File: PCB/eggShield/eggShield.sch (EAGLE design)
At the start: 34 parts, among them U1 V_REG_LDOSMD, U2 V_REG_LDOSMD

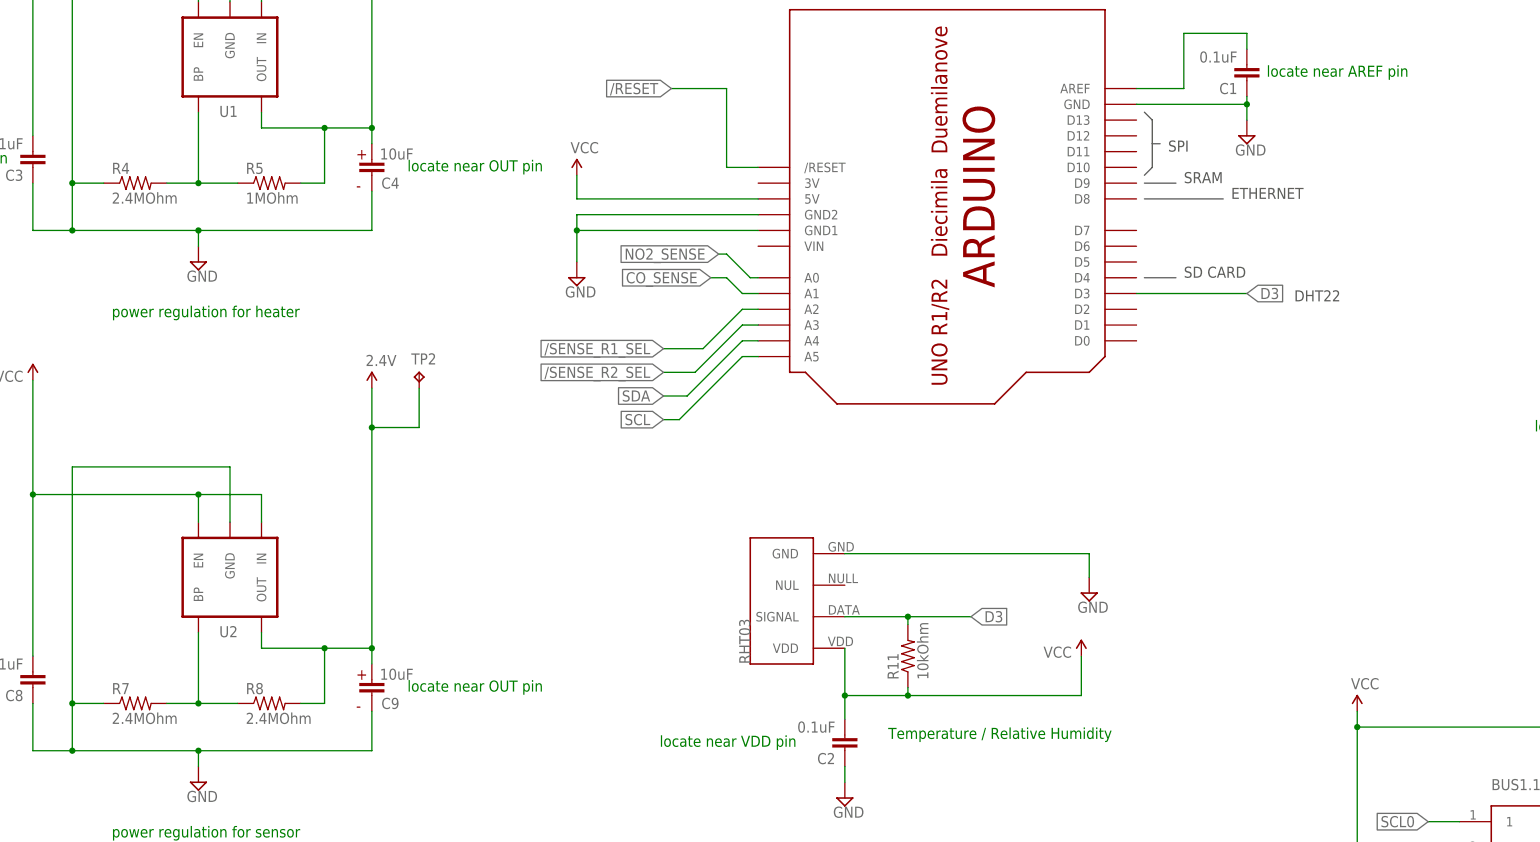
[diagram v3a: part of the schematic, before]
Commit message: changed DHT22 I/O to DIG2, changed LDO feedback resistor values again,  added more documentation to the schematic
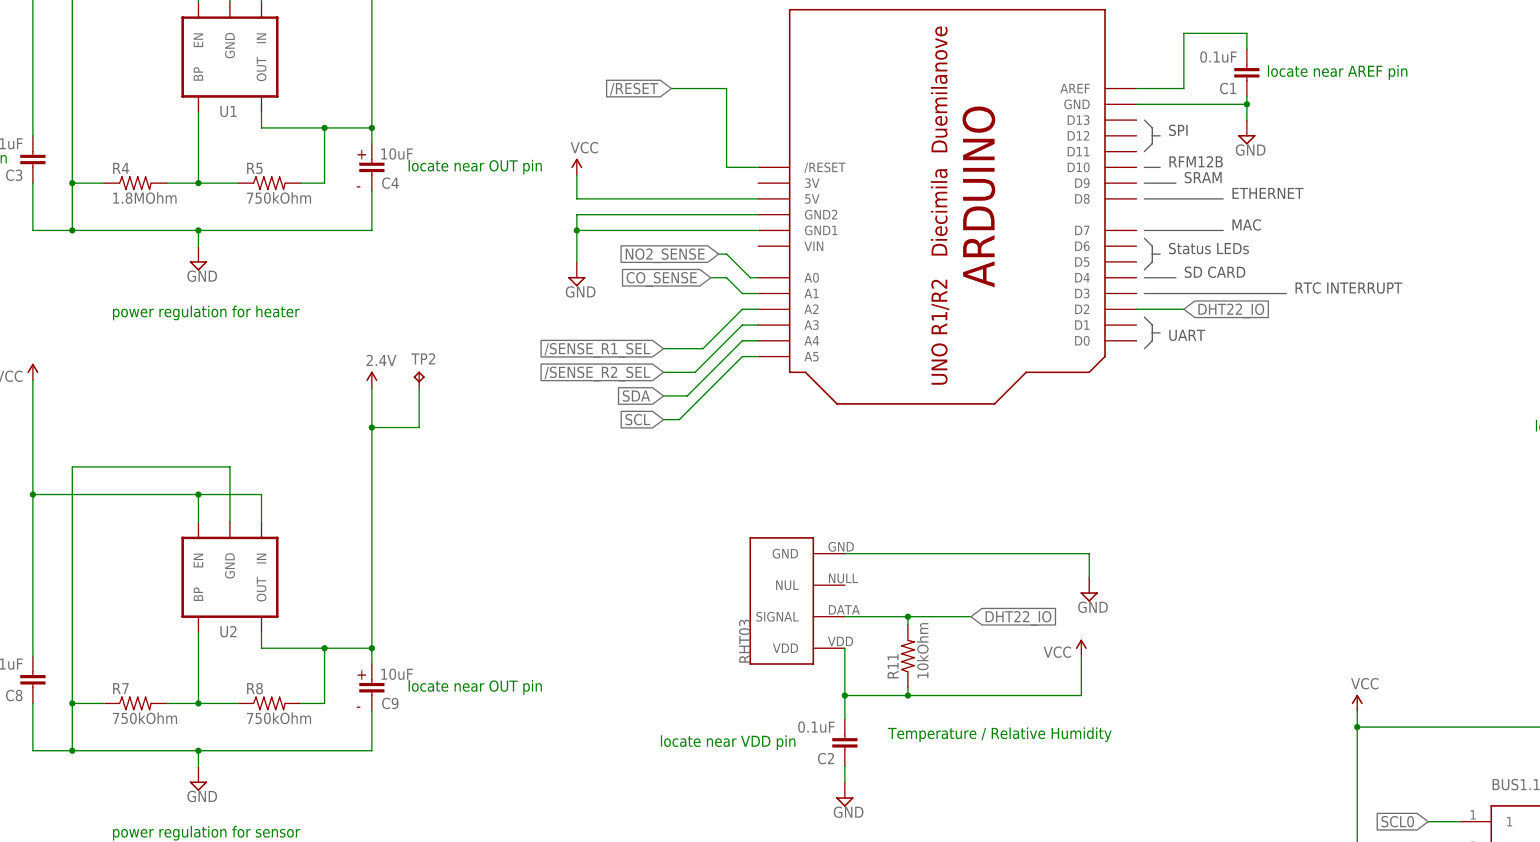
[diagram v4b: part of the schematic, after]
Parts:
- R4: value 2.4MOhm -> 1.8MOhm
- R5: value 1MOhm -> 750kOhm
- R7, R8: value 2.4MOhm -> 750kOhm
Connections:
- removed net D3: DHT22.SIGNAL, R11.2, U$7.D3
- new net DHT22_IO: DHT22.SIGNAL, R11.2, U$7.D2
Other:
- note added: "MAC"
- note added: "RFM12B"
- note added: "RTC INTERRUPT"
- note added: "Status LEDs"
- note added: "UART"
- note removed: "DHT22"

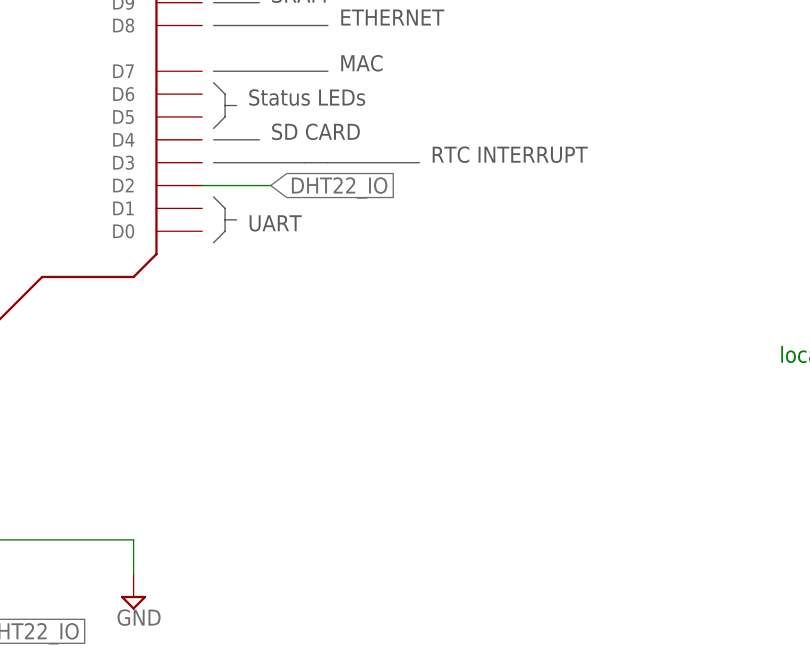
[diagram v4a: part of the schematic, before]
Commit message: added registration holes
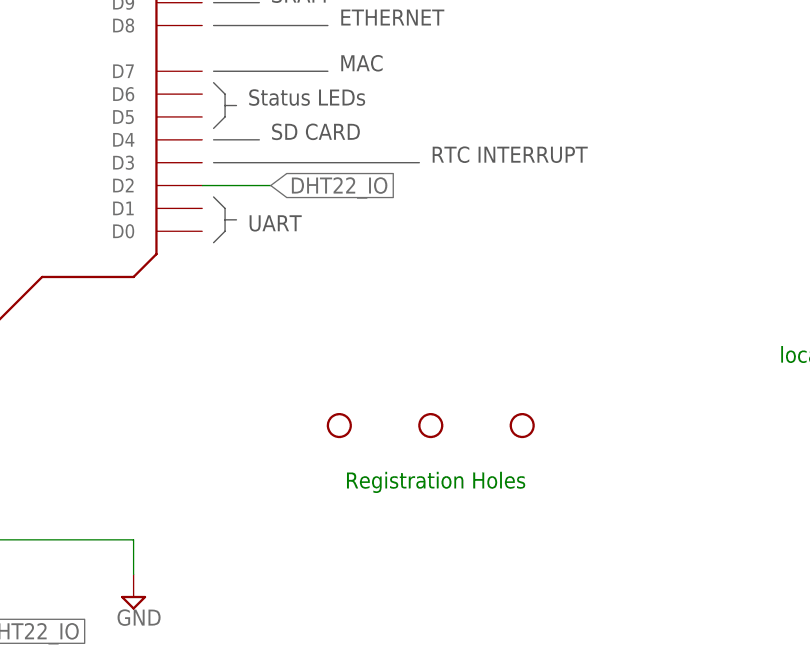
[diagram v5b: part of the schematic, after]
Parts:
- added JP1, JP2, JP3: STAND-OFF, SparkFun:STAND-OFF
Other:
- note added: "Registration Holes"
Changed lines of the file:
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@@
 <part name="P+5" library="SparkFun" deviceset="VCC" device=""/>
 <part name="SUPPLY11" library="supply2" deviceset="GND" device=""/>
+<part name="JP1" library="SparkFun" deviceset="STAND-OFF" device=""/>
+<part name="JP2" library="SparkFun" deviceset="STAND-OFF" device=""/>
+<part name="JP3" library="SparkFun" deviceset="STAND-OFF" device=""/>
 </parts>
 <sheets>
@@
 <wire x1="209.55" y1="210.82" x2="212.09" y2="210.82" width="0.1524" layer="97"/>
 <text x="213.36" y="210.82" size="1.778" layer="97">RFM12B</text>
-<wire x1="209.55" y1="190.5" x2="219.71" y2="190.5" width="0.1524" layer="97"/>
-<wire x1="219.71" y1="190.5" x2="222.25" y2="190.5" width="0.1524" layer="97"/>
-<wire x1="222.25" y1="190.5" x2="232.41" y2="190.5" width="0.1524" layer="97"/>
+<wire x1="209.55" y1="190.5" x2="232.41" y2="190.5" width="0.1524" layer="97"/>
 <text x="233.68" y="190.5" size="1.778" layer="97">RTC INTERRUPT</text>
 <wire x1="209.55" y1="186.69" x2="210.82" y2="185.42" width="0.1524" layer="97"/>
@@
 <wire x1="210.82" y1="184.15" x2="212.09" y2="184.15" width="0.1524" layer="97"/>
 <text x="213.36" y="182.88" size="1.778" layer="97">UART</text>
+<text x="224.155" y="154.305" size="1.778" layer="91">Registration Holes</text>
 </plain>
 <instances>
@@
 <instance part="P+5" gate="1" x="243.84" y="123.19"/>
 <instance part="SUPPLY11" gate="GND" x="254" y="74.93"/>
+<instance part="JP1" gate="G$1" x="223.52" y="161.29"/>
+<instance part="JP2" gate="G$1" x="233.68" y="161.29"/>
+<instance part="JP3" gate="G$1" x="243.84" y="161.29"/>
 </instances>
 <busses>

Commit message: major changes incorporating a heater co-processor
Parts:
- removed JP1, JP2: STAND-OFF, SparkFun:STAND-OFF
- removed R5, R8: 750kOhm, SparkFun:RESISTOR0805-RES
- removed RST: (no value), SparkFun:TAC_SWITCHSMD
- added C6, C7: 0.1uF, SparkFun:CAP0603-CAP
- added HEATER_CTRL: ATTINY45, SparkFun-DigitalIC:ATTINY45
- added R14, R15, R16, R17: 1.8kOhm, SparkFun:RESISTOR0805-RES
- added R18, R19: (no value), SparkFun:RESISTOR0805-RES
- added U3: MCP42XXX, SparkFun-AnalogIC:MCP42XXX
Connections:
- removed net N$1: R4.2, R5.1, U1.BP
- removed net N$2: R7.2, R8.1, U2.BP
- new net /POT_CS: HEATER_CTRL.PB5(NRES), U3.CS
- new net CO_FEEDBACK: CO.GND_HEATER, HEATER_CTRL.PB4(ADC2), R19.2
- new net CO_MISO: HEATER_CTRL.PB1(MISO), U3.DO
- new net CO_MOSI: HEATER_CTRL.PB0(MOSI), U3.DI
- new net CO_RH-: R4.2, U1.BP, U3.W1
- new net CO_SCK: HEATER_CTRL.PB2(SCK/ADC1), U3.SCK
- new net MISO: U$7.D12
- new net MOSI: U$7.D11
- new net NO2_FEEDBACK: HEATER_CTRL.PB3(ADC3), N02.GND_HEATER, R18.2
- new net NO2_RH-: R7.2, U2.BP, U3.W0
- new net SCK: U$7.D13
- net /RESET: no longer RST.1, RST.2
- net 1.7V: now also U3.A1; no longer R5.2
- net 2.4V: now also U3.A0; no longer N02.VSENS+, R8.2
- net GND: now also C6.1, C7.1, HEATER_CTRL.GND, R18.1, R19.1, U3.GND; no longer CO.GND_HEATER, N02.GND_HEATER, RST.3, RST.4
- net SCL0: now also R15.1
- net SCL1: now also R17.1
- net SDA0: now also R14.1
- net SDA1: now also R16.1
- net VCC: now also C6.2, C7.2, HEATER_CTRL.VCC, N02.VSENS+, R14.2, R15.2, R16.2, R17.2, U3.SHTDWN, U3.VCC
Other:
- note added: "Do not populate - Nanode has these two resistors already"
- note added: "NC"
- note added: "locate near VCC pin"
- note removed: "Do not populate - Nanode has these resistors already"
- note removed: "RTC INTERRUPT"
- moved on the sheet: BUS1.1, BUS1.2, BUS2.1, BUS2.2, C1, C5, I2CMUX, R12, R13

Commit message: incorporated several changes based on review comments
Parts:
- removed HEATER_CTRL: ATTINY45, SparkFun-DigitalIC:ATTINY45
- added C10: 0.1uF, SparkFun:CAP0603-CAP
- added C11, C12: 1uF, SparkFun:CAP0603-CAP
- added INFO: GREEN, adafruit:LEDCHIPLED_0805
- added L1: FERRITE, nanodeRF_11:RCL_R-EU_R0805
- added MCU: ATTINY4832A, axeio-SparkFun:ATTINY4832A
- added PWR: RED, adafruit:LEDCHIPLED_0805
- added R5: 270ohm, SparkFun:RESISTOR0805-RES
- added R8: 470ohm, SparkFun:RESISTOR0805-RES
- added U$13, U$14: PLANE_COUPLER, wicked-device:PLANE_COUPLER
- added VCC2_5: AP7333SA, wicked-device:AP7333SA
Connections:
- net 1.7V renamed NO2_HEATER_V
- net 2.4V renamed CO_HEATER_V
- removed net /SENSE_R1_SEL: R1.1, R2.2, R6.1, R9.2, U$7.A2
- removed net /SENSE_R2_SEL: R10.2, R2.1, R3.2, R9.1, U$7.A3
- removed net CO_MISO: HEATER_CTRL.PB1(MISO), U3.DO
- removed net CO_MOSI: HEATER_CTRL.PB0(MOSI), U3.DI
- removed net CO_SCK: HEATER_CTRL.PB2(SCK/ADC1), U3.SCK
- removed net VCC: BUS1.1.3, BUS1.2.3, BUS2.1.3, BUS2.2.3, C2.2, C3.2, C5.2, C6.2, C7.2, C8.2, CO.VSENS+, DHT22.VDD, HEATER_CTRL.VCC, I2CMUX.VDD, N02.VSENS+, R11.1, R12.2, R13.2, R14.2, R15.2, R16.2, R17.2, U$7.5V, U1.EN, U1.IN, U2.EN, U2.IN, U3.SHTDWN, U3.VCC
- new net /R1_SEL: MCU.PC7(PCINT15), R1.1, R2.2, R6.1, R9.2
- new net /R2_SEL: MCU.PA0(ADC6/PCINT24), R10.2, R2.1, R3.2, R9.1
- new net 5V: BUS1.1.3, BUS1.2.3, BUS2.1.3, BUS2.2.3, C2.2, C3.2, C5.2, C6.1, C7.2, C8.2, CO.VSENS+, DHT22.VDD, I2CMUX.VDD, L1.2, MCU.VCC, R11.1, R12.2, R13.2, R14.2, R15.2, R16.2, R17.2, U$7.5V, U1.IN, U2.IN, U3.SHTDWN, U3.VCC
- new net AGND: C10.2, C11.2, C12.2, MCU.GND2, R10.1, R18.1, R19.1, R3.1, U$13.P$1, VCC2_5.GND
- new net AVCC: C10.1, L1.1, MCU.AVCC
- new net CO_HEATER_EN: U2.EN
- new net MISO_B: MCU.PB4(PCINT4/MISO), U3.DO
- new net MOSI_B: MCU.PB3(PCINT3/MOSI), U3.DI
- new net N$1: INFO.A, R5.1
- new net N$2: C11.1, VCC2_5.VI
- new net N$3: PWR.A, R8.1
- new net NO2_HEATER_EN: MCU.PD0(PCINT16), U1.EN
- new net NO2_OPERATING_V: C12.1, N02.VSENS+, VCC2_5.VO
- new net POWER: MCU.PB2(PCINT2/SS/OC1B), R8.2
- new net RETURN_GND: U$13.P$2, U$14.P$2, U$7.GND1, U$7.GND2
- new net SCK_B: MCU.PB5(SCK/PCINT5), U3.SCK
- new net STATUS: MCU.PB1(PCINT1/OC1A), R5.2
- net /POT_CS: now also MCU.PD2(INT0/PCINT18); no longer HEATER_CTRL.PB5(NRES)
- net /RESET: now also MCU.PC6(RESET/PCINT14)
- net CO_FEEDBACK: now also MCU.PC3(ADC3/PCINT11); no longer HEATER_CTRL.PB4(ADC2)
- net CO_RH-: now also R7.2, U2.BP; no longer R4.2, U1.BP
- net CO_SENSE: now also MCU.PC2(ADC2/PCINT10); no longer U$7.A1
- net GND: now also C6.2, INFO.C, MCU.GND1, PWR.C, U$14.P$1; no longer C6.1, HEATER_CTRL.GND, R10.1, R18.1, R19.1, R3.1, U$7.GND1, U$7.GND2
- net NO2_FEEDBACK: now also MCU.PC1(ADC1/PCINT9); no longer HEATER_CTRL.PB3(ADC3)
- net NO2_RH-: now also R4.2, U1.BP; no longer R7.2, U2.BP
- net NO2_SENSE: now also MCU.PC0(ADC0/PCINT8); no longer U$7.A0
- net SCL: now also MCU.PC5(ADC5/SCL/PCINT13)
- net SDA: now also MCU.PC4(ADC4/SDA/PCINT12)
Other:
- note added: "2.5V"
- note added: "analog power filtering"
- note added: "locate near AVCC pin"
- note added: "star topology for separating analog and digital GND"
- moved on the sheet: BUS1.1, BUS1.2, BUS2.1, BUS2.2, C1, C2, C5, C6, C7, I2CMUX, R1, R10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

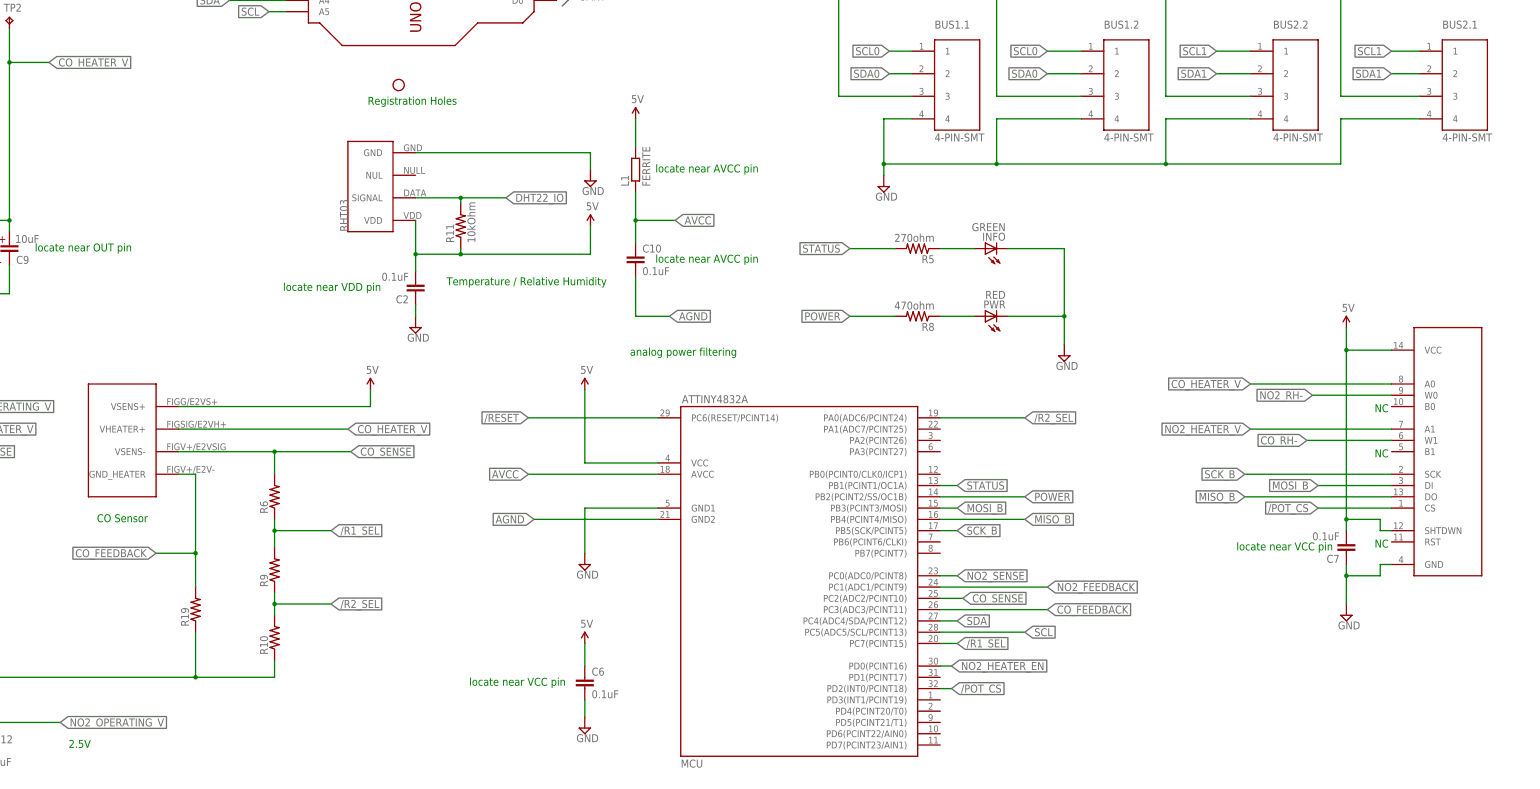
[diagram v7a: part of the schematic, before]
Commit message: updated to make it possible to shut down heaters from coprocessor, added programming header, added analog inputs to measure heater V+, and moved /R2_SEL to accomodate
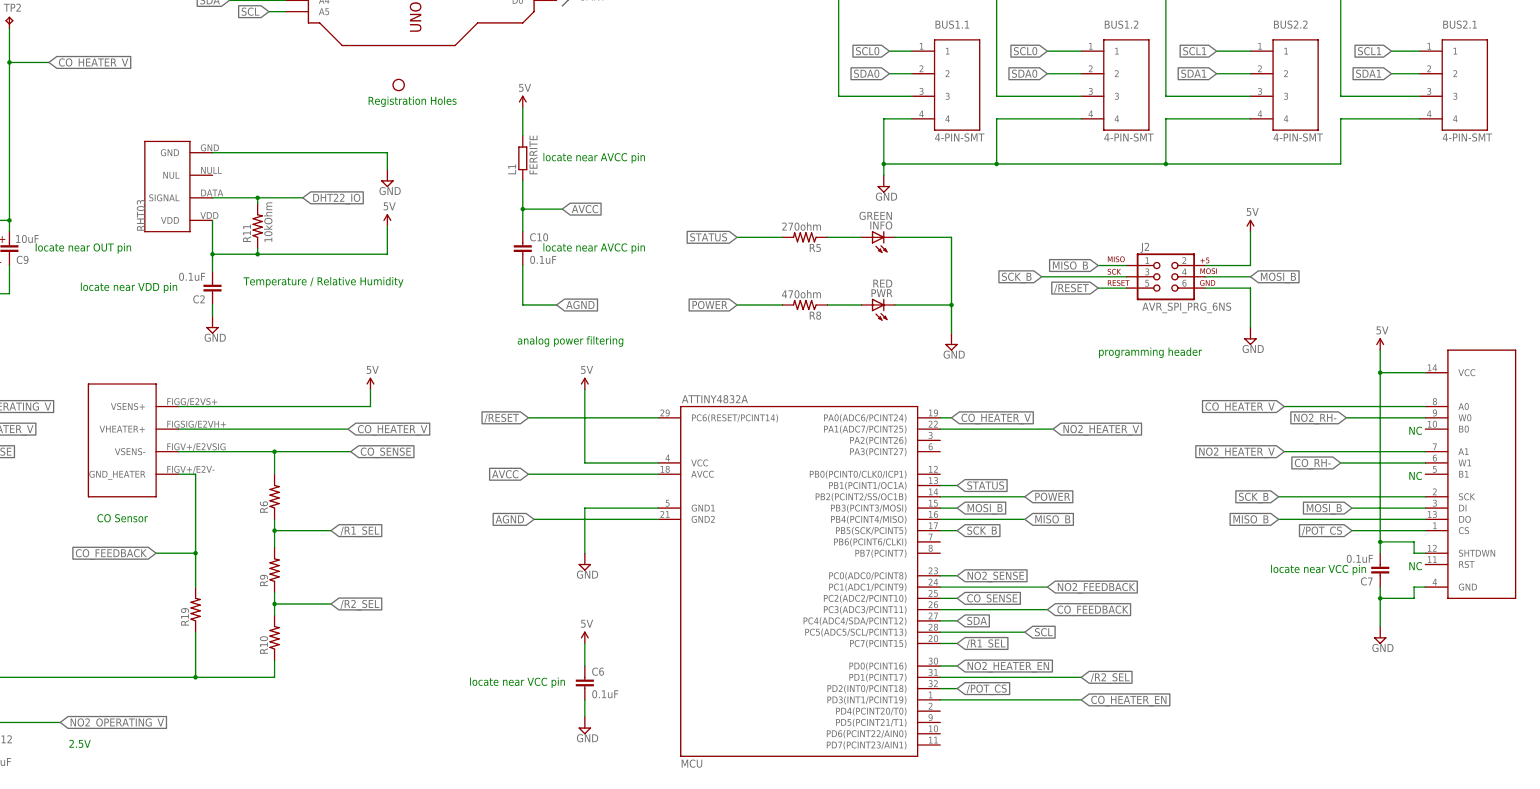
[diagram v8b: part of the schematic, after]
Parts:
- added J2: AVR_SPI_PRG_6NS, SparkFun:AVR_SPI_PRG_6NS
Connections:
- net /R2_SEL: now also MCU.PD1(PCINT17); no longer MCU.PA0(ADC6/PCINT24)
- net /RESET: now also J2.5
- net 5V: now also J2.2
- net CO_HEATER_EN: now also MCU.PD3(INT1/PCINT19)
- net CO_HEATER_V: now also MCU.PA0(ADC6/PCINT24)
- net GND: now also J2.6
- net MISO_B: now also J2.1
- net MOSI_B: now also J2.4
- net NO2_HEATER_V: now also MCU.PA1(ADC7/PCINT25)
- net SCK_B: now also J2.3
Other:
- note added: "programming header"
- moved on the sheet: C10, C2, C7, INFO, L1, PWR, R11, R5, R8
